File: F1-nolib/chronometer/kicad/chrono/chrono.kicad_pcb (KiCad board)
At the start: 2 copper layers, 95 x 54.5 mm, 66 parts, among them J1 Power 12V, J2 +5Vout, J3 Ext_trig0, J4 LIDAR, J5 Ext_trig1, J6 Ext_trig2, J7 USART1, P1 USB_B, Q1 AO3407, Q2 DTA114Y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

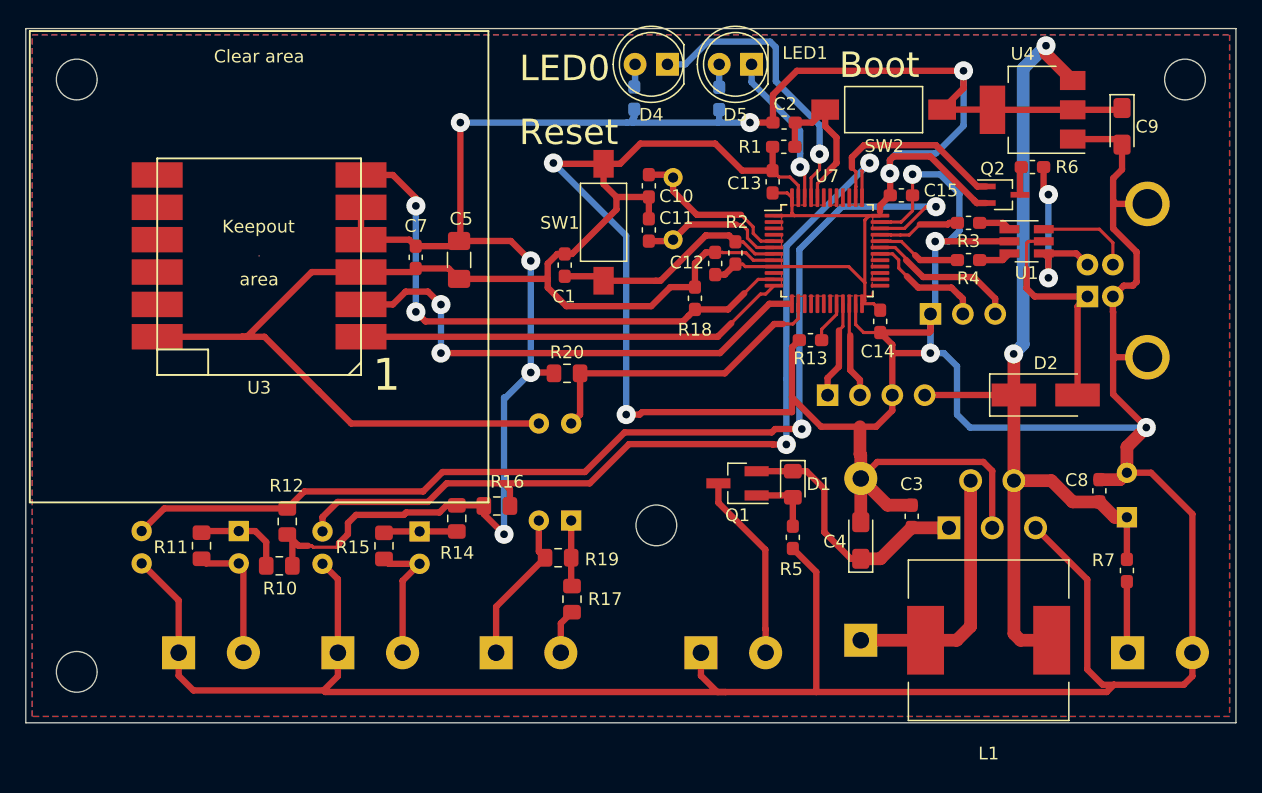
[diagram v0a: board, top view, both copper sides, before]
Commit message: add chrono v2
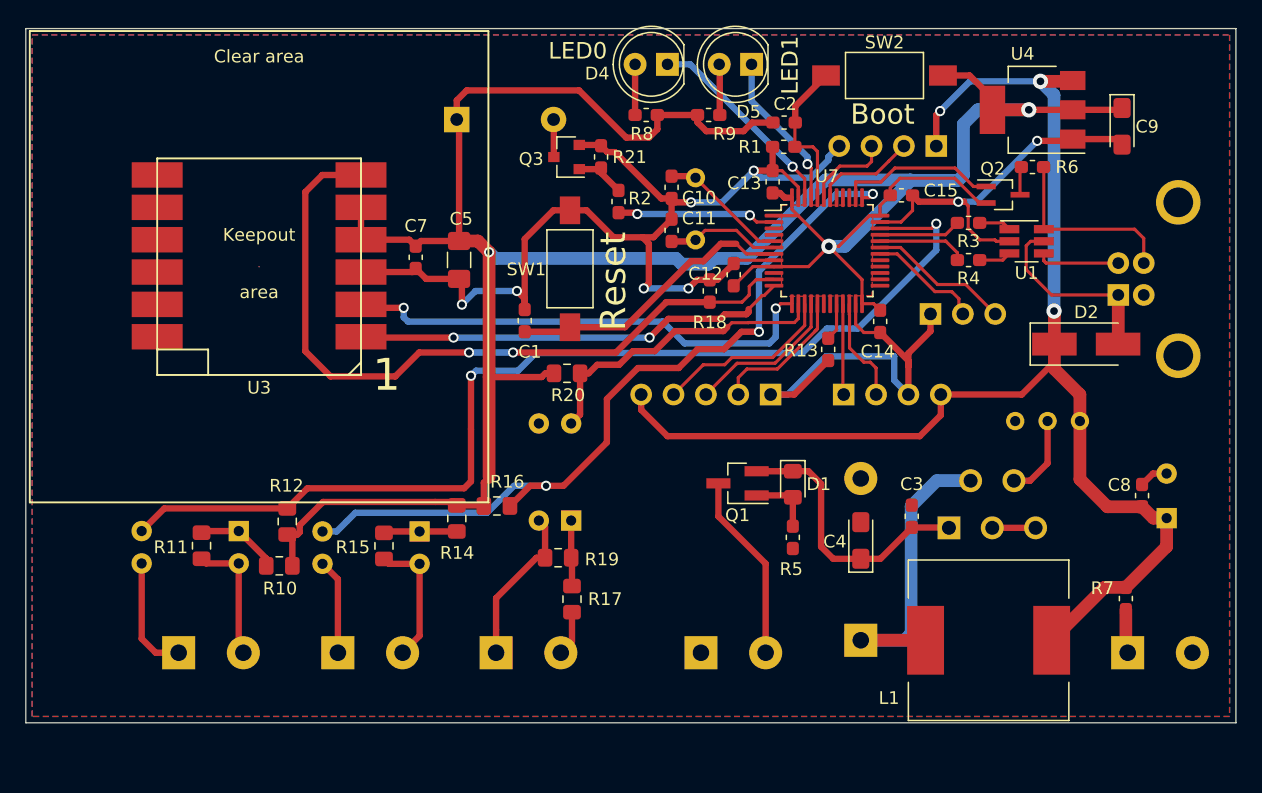
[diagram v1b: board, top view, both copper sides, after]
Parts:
- removed REF** (x4): MountingHole_3.2mm_M3, MountingHole:MountingHole_3.2mm_M3
- added BZ1: Buzzer, Buzzer_Beeper:Buzzer_12x9.5RM7.6, B.Cu at (81.3, 50.1)
- added J8: SPI, Connector_PinSocket_2.54mm:PinSocket_1x05_P2.54mm_Vertical, B.Cu at (106.0, 71.7)
- added J9: I2C1, Connector_PinSocket_2.54mm:PinSocket_1x04_P2.54mm_Vertical, B.Cu at (119.0, 52.2)
- added Q3: Q_NMOS_GSD, Package_TO_SOT_SMD:SOT-23, F.Cu at (90.0, 53.1)
- added R21: 10k, Resistor_SMD:R_0603_1608Metric_Pad1.05x0.95mm_HandSolder, F.Cu at (92.7, 53.1)
- added RV1: 10k, Potentiometer_THT:Potentiometer_Bourns_3296W_Vertical, B.Cu at (130.3, 73.8)
- R2: value 10k -> 510
- R8, R9: moved to F.Cu
- U2: value LM2576HV -> LM2576ADJ
- moved R2 10.0 mm to (94.0, 56.6)
- moved C1 5.37 mm to (86.7, 65.9)
- moved D2 5.11 mm to (130.7, 67.8)
- moved SW1 4.50 mm to (90.2, 61.9)
- moved C8 3.37 mm to (135.1, 79.7)
- moved C6 3.12 mm to (137.1, 81.4)
- moved SW2 2.68 mm to (114.9, 46.7)
- moved P1 2.43 mm to (133.3, 63.9)
- moved R7 2.20 mm to (133.9, 87.7)
- moved C10 1.79 mm to (98.2, 55.5)
- moved C11 1.79 mm to (98.2, 58.8)
- moved Y1 1.76 mm to (100.1, 54.7)
- moved C12 1.70 mm to (103.1, 62.3)
- moved R8 1.62 mm to (96.2, 49.8), turned to 0 degrees
- moved R13 1.57 mm to (110.5, 68.2), turned to 270 degrees
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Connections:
- R2 pad 1: /NRST -> Net-(Q3-Pad1)
- R2 pad 2: +3V3 -> /buzzer
- R6 pad 2: Net-(P1-Pad2) -> Net-(P1-Pad3)
- U2 pad 4: +5V -> Net-(RV1-Pad2)
- U7 pad 15: (no net) -> /SCK
- U7 pad 16: (no net) -> /MISO
- U7 pad 17: (no net) -> /MOSI
- U7 pad 2: (no net) -> /buzzer
- U7 pad 42: (no net) -> /SCL
- U7 pad 43: (no net) -> /SDA
- U7 pad 45: /LED0 -> /LED1
- U7 pad 46: /LED1 -> /LED0
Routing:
- net GND: track 465.2 -> 171.0 mm, vias 6 -> 8
- net +5V: track 74.4 -> 108.4 mm, vias 2 -> 3
- net +3V3: track 196.6 -> 222.1 mm, vias 7 -> 3
- net /PPS: track 43.8 -> 58.6 mm
- net /SCK: track 0.00 -> 14.3 mm
- net /buzzer: track 0.00 -> 12.5 mm, vias 0 -> 2
- net /MISO: track 0.00 -> 12.3 mm
- net /MOSI: track 0.00 -> 11.3 mm
- net Net-(P1-Pad2): track 14.7 -> 6.50 mm, vias 2 -> 0
- net /SCL: track 0.00 -> 8.06 mm
- net Net-(P1-Pad3): track 7.59 -> 15.0 mm
- net /LED0: track 22.9 -> 16.0 mm
- net /SDA: track 0.00 -> 6.85 mm
- net Net-(RV1-Pad2): track 0.00 -> 6.52 mm
- net /TRIG1: track 69.7 -> 63.4 mm, vias 2 -> 3
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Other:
- net class Default: via_dia 1.5 -> 0.8; via_drill 0.6 -> 0.5
- board text added: "+5 GND Rx Tx"
- board text added: "+5 SCL SDA GND"
- board text added: "GND MOSI MISO SCK +5V"
- board text added: "I2C"
- board text added: "LIDAR"
- board text added: "Rx Tx GND"
- board text added: "SPI"
- board text added: "USART1"
- board text added: "gnd +5V out"
- board text removed: "+5V out"
